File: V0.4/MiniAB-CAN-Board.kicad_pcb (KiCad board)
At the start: 4 copper layers, 51.1 x 45.2 mm, 128 parts, among them J1 PCF, J10 USB_B_Micro, J11 CAN, J12 ENDSTOP1, J13 ENDSTOP2, J14 PROBE, J2 PCF, J3 HEF, J4 TH0, J5 I2C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

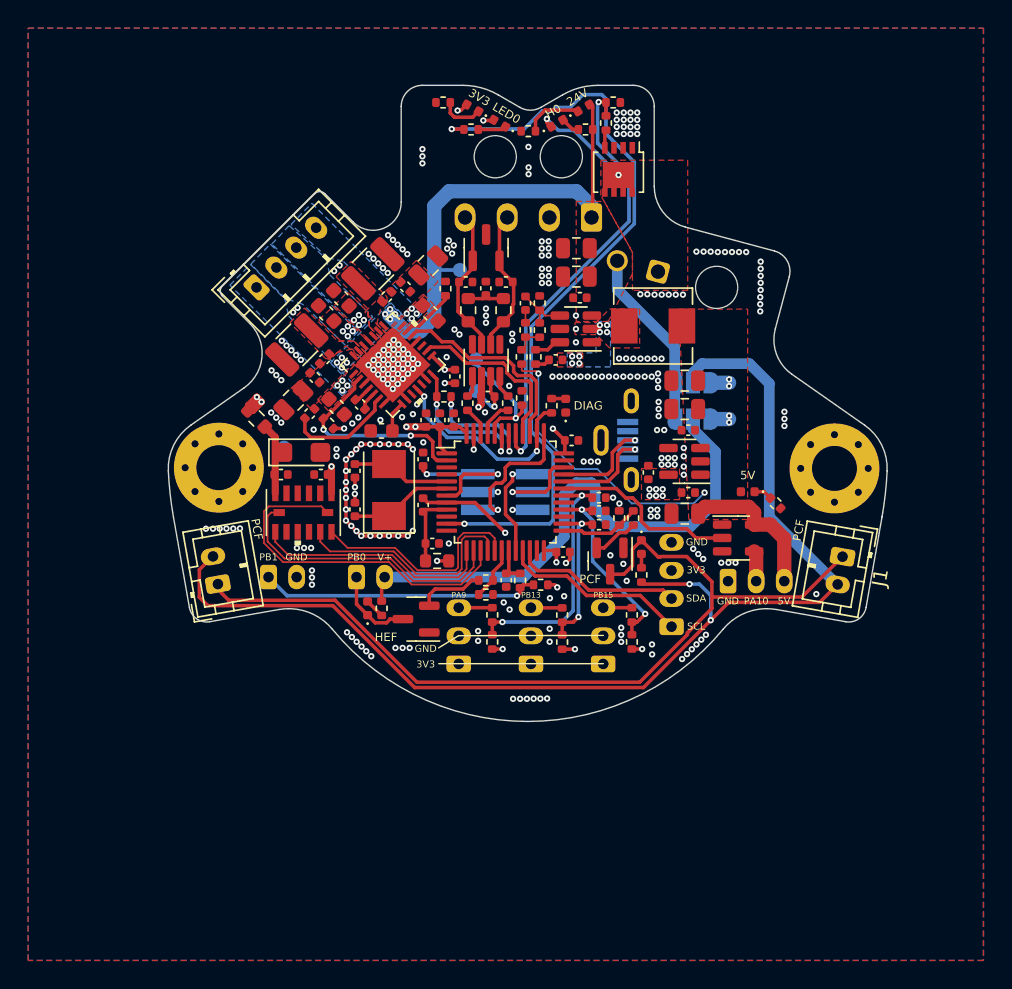
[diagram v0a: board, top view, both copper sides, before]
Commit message: add polarity check, change crystal, change debug, add buttons, exchange 5V regulator, correct MOSFETs, updated TMC2209 and all capacitors
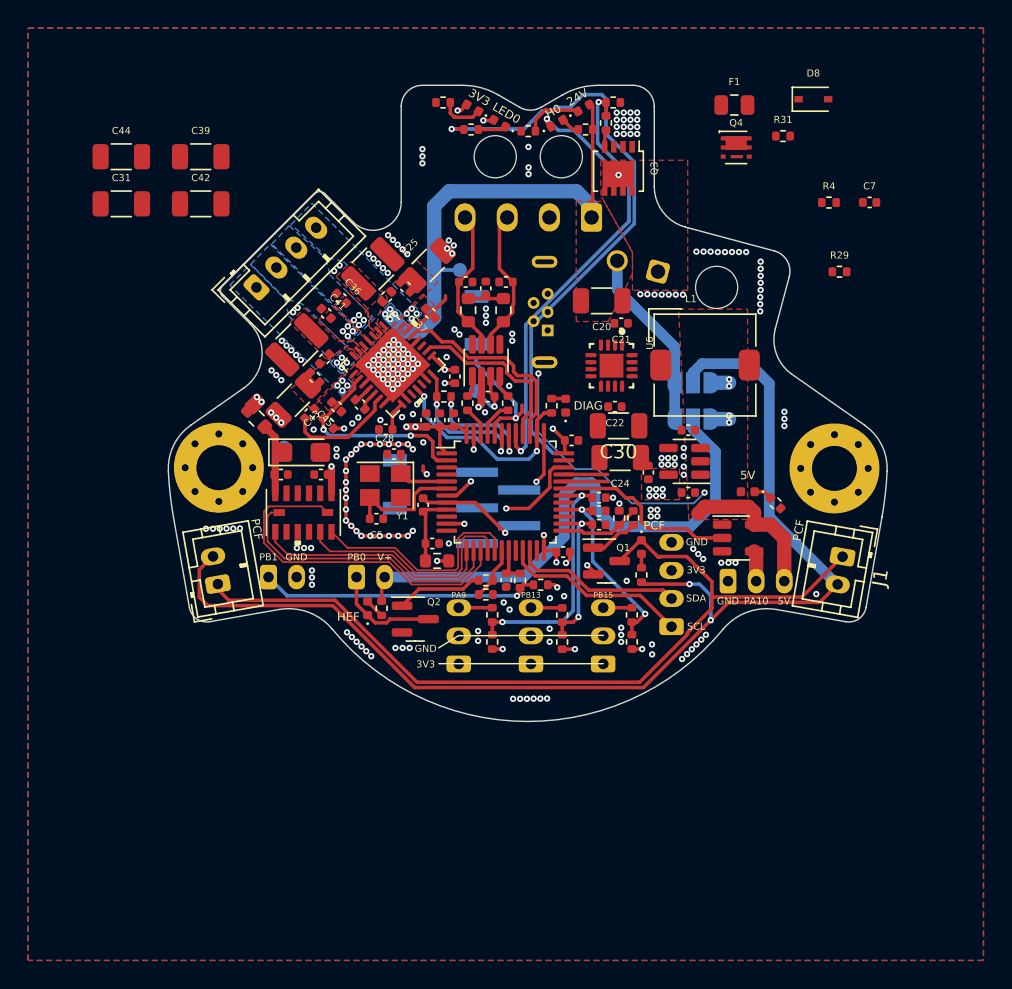
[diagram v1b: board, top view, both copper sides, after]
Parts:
- removed C49, C51: 22u, Capacitor_SMD:C_0805_2012Metric
- removed L2: 6.8u, Inductor_SMD:L_Sunlord_MWSA0518_5.4x5.2mm
- removed R32: 10k, Resistor_SMD:R_0402_1005Metric
- removed R35: 100k, Resistor_SMD:R_0402_1005Metric
- removed R36: 49.9, Resistor_SMD:R_0402_1005Metric
- removed R37: 0, Resistor_SMD:R_0402_1005Metric
- removed TP1: BOOT0, TestPoint:TestPoint_Pad_D1.0mm
- added C31: 10u/35V, Capacitor_SMD:C_1206_3216Metric, F.Cu at (185.1, 53.0)
- added C39: 10u/35V, Capacitor_SMD:C_1206_3216Metric, F.Cu at (190.7, 49.6)
- added C44: 10u/35V, Capacitor_SMD:C_1206_3216Metric, F.Cu at (185.1, 49.6)
- added F1: 3.5A, Fuse:Fuse_0805_2012Metric, F.Cu at (228.7, 46.0)
- added L1: 4.7u, Inductor_SMD:L_TDK_SLF7045, F.Cu at (226.6, 64.5)
- added Q4: SiA449DJ, Package_TO_SOT_SMD:Vishay_PowerPAK_SC70-6L_Single, F.Cu at (228.8, 49.0)
- added SW1: RESET, Button_Switch_SMD:SW_SPST_B3U-1000P, B.Cu at (204.5, 73.0)
- added SW2: BOOT0, Button_Switch_SMD:SW_SPST_B3U-1000P, B.Cu at (210.3, 61.3)
- C2, C5: value 20p -> 12p
- C20: value 10p -> 10u/35V; footprint Capacitor_SMD:C_0402_1005Metric -> Capacitor_SMD:C_1206_3216Metric
- C21: value 10u/35V -> 100n/35V; footprint Capacitor_SMD:C_0805_2012Metric -> Capacitor_SMD:C_0402_1005Metric
- C22: value 22u -> 22n; footprint Capacitor_SMD:C_0805_2012Metric -> Capacitor_SMD:C_0402_1005Metric
- C24: value 10u/35V -> 22u; footprint Capacitor_SMD:C_0805_2012Metric -> Capacitor_SMD:C_1206_3216Metric
- C25, C43: value 100u/35V, Low ESR -> 10u/35V; footprint Capacitor_SMD:C_0805_2012Metric -> Capacitor_SMD:C_1206_3216Metric
- C28: value 2.2u/16V -> 4.7u; footprint Capacitor_SMD:C_0603_1608Metric -> Capacitor_SMD:C_0402_1005Metric
- C30: value 100n/35V -> 22u; footprint Capacitor_SMD:C_0402_1005Metric -> Capacitor_SMD:C_1206_3216Metric
- C36, C37, C41, C45: value 470p/100V -> 1n/50V; footprint Capacitor_SMD:C_0603_1608Metric -> Capacitor_SMD:C_0402_1005Metric
- C42: value 100n -> 10u/35V; footprint Capacitor_SMD:C_0402_1005Metric -> Capacitor_SMD:C_1206_3216Metric
- C47: value 100n, 6.3V -> 100n
- D8: value SZNUP2105L -> 15V; footprint Package_TO_SOT_SMD:SOT-23 -> Diode_SMD:D_SOD-323
- J10: footprint Connector_USB:USB_Micro-B_Molex-105133-0001 -> Connector_USB:USB_Micro-B_Wuerth_614105150721_Vertical
- J9: footprint Connector_PinHeader_1.27mm:PinHeader_2x03_P1.27mm_Vertical_SMD -> Connector_PinHeader_1.27mm:PinHeader_1x05_P1.27mm_Vertical_SMD_Pin1Left
- R11: value 2.2k -> 2.2k 0.1%
- R29: value 30 -> 100k
- R31: value 52.3k -> 100k
- U6: value TPS56339DDC -> TS30041-M050QFNR; footprint Package_TO_SOT_SMD:SOT-23-6 -> TS30041:Semtech-QFN16-0-0-0
- Y1: footprint Crystal:Crystal_SMD_5032-2Pin_5.0x3.2mm -> Crystal:Crystal_SMD_3225-4Pin_3.2x2.5mm
- moved C7 36.6 mm to (238.3, 52.9), turned to 0 degrees
- moved C42 27.6 mm to (190.7, 53.0), turned to 0 degrees
- moved R4 25.9 mm to (235.4, 52.9), turned to 0 degrees
- moved D8 25.6 mm to (234.3, 45.6), turned to 0 degrees
- moved R29 22.5 mm to (236.1, 57.8), turned to 0 degrees
- moved R31 22.1 mm to (232.1, 48.2), turned to 0 degrees
- moved C24 13.2 mm to (220.5, 71.0)
- moved C30 9.52 mm to (220.4, 68.8)
- moved J10 9.21 mm to (215.4, 62.0)
- moved C22 9.09 mm to (220.2, 67.4)
- moved C21 6.22 mm to (220.6, 61.5)
- moved C20 5.42 mm to (219.2, 59.9), turned to 180 degrees
- moved U6 3.64 mm to (219.9, 64.5), turned to -90 degrees
- moved C2 3.02 mm to (204.4, 70.8), turned to 0 degrees
- moved C5 1.67 mm to (203.2, 75.4), turned to 180 degrees
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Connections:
- net Net-(R4-Pad2) renamed BOOT0
- C20 pad 1: Net-(C20-Pad1) -> TMC_VS
- C20 pad 2: /FB -> GND
- C22 pad 1: +5V -> Net-(C22-Pad1)
- C22 pad 2: GND -> Net-(C22-Pad2)
- C24 pad 1: TMC_VS -> +5V
- C28 pad 1: Net-(C28-Pad1) -> GND
- C28 pad 2: GND -> Net-(U5-Pad8)
- C30 pad 1: TMC_VS -> +5V
- C42 pad 1: /SW -> TMC_VS
- C42 pad 2: Net-(C42-Pad2) -> GND
- C5 pad 1: OSC_OUT -> GND
- C5 pad 2: GND -> OSC_OUT
- C7 pad 1: GND -> RESET
- C7 pad 2: NRST -> GND
- D8 pad 1: CANH -> TMC_VS
- D8 pad 2: CANL -> Net-(D8-Pad2)
- J11 pad 1: TMC_VS -> PWR
- J9 pad 1: SWCLK -> GND
- J9 pad 2: GND -> VBAT
- J9 pad 3: VBAT -> SWDIO
- J9 pad 4: SWDIO -> SWCLK
- J9 pad 5: NRST -> RESET
- Q1 pad 1: GND -> Net-(R2-Pad1)
- Q1 pad 2: Net-(Q1-Pad2) -> GND
- Q2 pad 1: GND -> Net-(Q2-Pad1)
- Q2 pad 2: Net-(Q2-Pad2) -> GND
- R1 pad 2: PC-FAN -> Net-(R2-Pad1)
- R14 pad 1: ENDSTOP1 -> Net-(J12-Pad3)
- R18 pad 1: ENDSTOP2 -> Net-(J13-Pad3)
- R2 pad 1: Net-(Q1-Pad2) -> Net-(R2-Pad1)
- R21 pad 1: PROBE -> Net-(J14-Pad3)
- R22 pad 1: Net-(J14-Pad3) -> PROBE
- R22 pad 2: PROBE -> Net-(J14-Pad3)
- R29 pad 1: /BOOT -> RESET
- R29 pad 2: Net-(C42-Pad2) -> VBAT
- R31 pad 1: /FB -> GND
- R31 pad 2: Net-(R31-Pad2) -> Net-(D8-Pad2)
- R5 pad 2: HE-FAN -> Net-(Q2-Pad1)
- R6 pad 1: Net-(Q2-Pad2) -> Net-(Q2-Pad1)
- R8 pad 2: HEATER -> Net-(Q3-Pad2)
- U2 pad 7: NRST -> RESET
- U5 pad 20: Net-(R35-Pad1) -> unconnected-(U5-Pad20)
- U5 pad 7: GND -> unconnected-(U5-Pad7)
- U5 pad 8: Net-(C28-Pad1) -> Net-(U5-Pad8)
- U6 pad 1: GND -> Net-(C22-Pad1)
- U6 pad 2: /SW -> TMC_VS
- U6 pad 4: /FB -> GND
- U6 pad 5: unconnected-(U6-Pad5) -> +5V
- U6 pad 6: /BOOT -> unconnected-(U6-Pad6)
- Y1 pad 1: OSC_OUT -> OSC_IN
- Y1 pad 2: OSC_IN -> GND
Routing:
- net LED0: track 55.2 -> 1.27 mm, vias 2 -> 1
- net HEATER: track 31.9 -> 74.6 mm, vias 2 -> 3
- net NRST: track 9.66 -> 0.00 mm, vias 2 -> 0
- net BOOT1: track 7.38 -> 0.00 mm, vias 1 -> 0
- net SWCLK: track 10.4 -> 3.65 mm
- net Net-(Q2-Pad1): track 0.00 -> 6.20 mm
- net Net-(Q2-Pad2): track 4.72 -> 0.00 mm
- net unconnected-(U5-Pad20): track 0.00 -> 3.93 mm
- net Net-(R35-Pad1): track 3.93 -> 0.00 mm
- net /FB: track 3.91 -> 0.00 mm
- net USB_DP: track 6.79 -> 3.12 mm, vias 1 -> 0
- net USB_DM: track 6.73 -> 3.16 mm, vias 1 -> 0
- net Net-(R2-Pad1): track 0.00 -> 3.27 mm
- net Net-(Q1-Pad2): track 3.27 -> 0.00 mm
- net PROBE: track 17.5 -> 19.9 mm
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- removed copper zone on B.Cu, net /SW
- removed copper zone on F.Cu, net /SW

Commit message: reduces CAN interface, complets USB interface, add new mounting holes
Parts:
- removed C29: 1n, Capacitor_SMD:C_0402_1005Metric
- removed C32, C33: 56p, Capacitor_SMD:C_0402_1005Metric
- removed R34: 1k, Resistor_SMD:R_0402_1005Metric
- added H3: MountingHole_Pad, MountingHole:MountingHole_3.2mm_M3_Pad_Via, F.Cu at (229.4, 56.3)
- added H4: MountingHole_Pad, MountingHole:MountingHole_3.2mm_M3_Pad_Via, F.Cu at (198.4, 87.2)
- added R32: 27, Resistor_SMD:R_0402_1005Metric, F.Cu at (244.6, 61.5)
- added U7: USBLC6-2SC6, Package_TO_SOT_SMD:SOT-23-6, F.Cu at (240.5, 62.8)
- R26: value 60 -> 1.5k; footprint Resistor_SMD:R_0603_1608Metric -> Resistor_SMD:R_0402_1005Metric
- R27: value 60 -> 120R; footprint Resistor_SMD:R_0603_1608Metric -> Resistor_SMD:R_0402_1005Metric
- R33: value 1k -> 27
- moved R26 30.6 mm to (242.3, 66.0), turned to 0 degrees
- moved R33 29.8 mm to (239.4, 66.0), turned to 0 degrees
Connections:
- J10 pad 1: unconnected-(J10-Pad1) -> Net-(J10-Pad1)
- J10 pad 2: USB_DM -> Net-(J10-Pad2)
- J10 pad 3: USB_DP -> Net-(J10-Pad3)
- J10 pad 6: unconnected-(J10-Pad6) -> GND
- R26 pad 1: CANL -> USB_DP
- R26 pad 2: Net-(C29-Pad1) -> VBAT
- R27 pad 1: Net-(C29-Pad1) -> CANL
- R33 pad 1: CAN_TX -> USB_DM
- U8 pad 1: Net-(R33-Pad2) -> CAN_TX
- U8 pad 4: Net-(R34-Pad2) -> CAN_RX
- U8 pad 5: GND -> unconnected-(U8-Pad5)
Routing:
- net GND: track 35.5 -> 110.1 mm, vias 235 -> 237
- net HEATER: track 74.6 -> 0.00 mm, vias 3 -> 1
- net Net-(C29-Pad1): track 3.21 -> 0.00 mm
- net CANL: track 10.4 -> 13.6 mm
- net PROBE: track 19.9 -> 17.5 mm
- net Net-(J14-Pad3): track 0.00 -> 2.39 mm
- net Net-(R34-Pad2): track 1.63 -> 0.00 mm
- net CAN_RX: track 2.57 -> 4.20 mm
- net Net-(R33-Pad2): track 1.54 -> 0.00 mm
- net CAN_TX: track 2.04 -> 3.57 mm
